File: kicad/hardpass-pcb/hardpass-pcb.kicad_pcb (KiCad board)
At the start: 2 copper layers, 80 x 65 mm, 61 parts, among them P1 Pi_Zero, P2 OLED_I2C, P3 Pi_Zero, SW1 1, SW10 C/UP, SW11 0/OK, SW12 OK/DN, SW2 2, SW3 3, SW4 4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

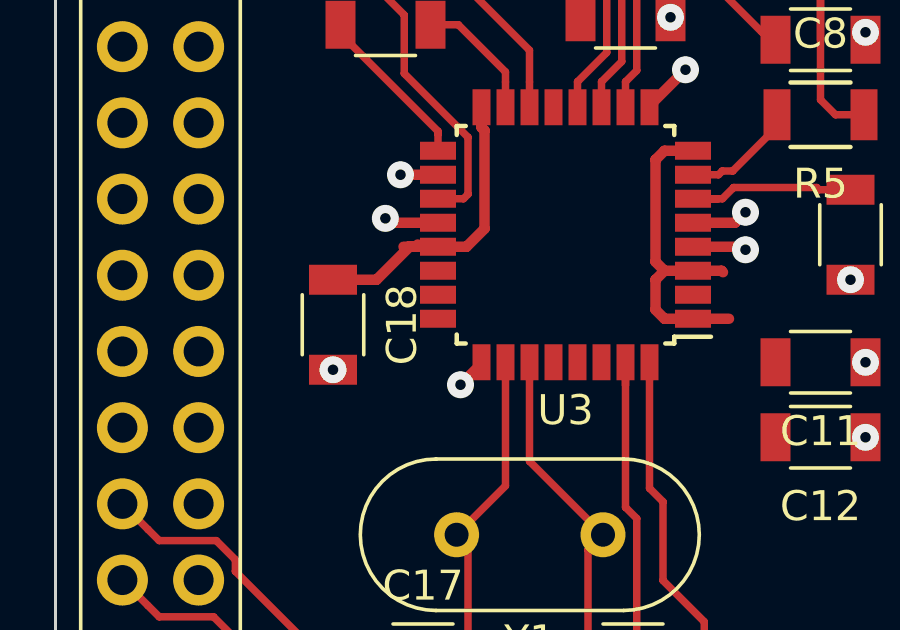
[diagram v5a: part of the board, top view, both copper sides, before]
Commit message: fixed bug (shdn_N), removed caps
according to data sheet, shdn_n needs to be high to activate card (page43)

2 bypass caps have been removed according to page 8 of AN00046
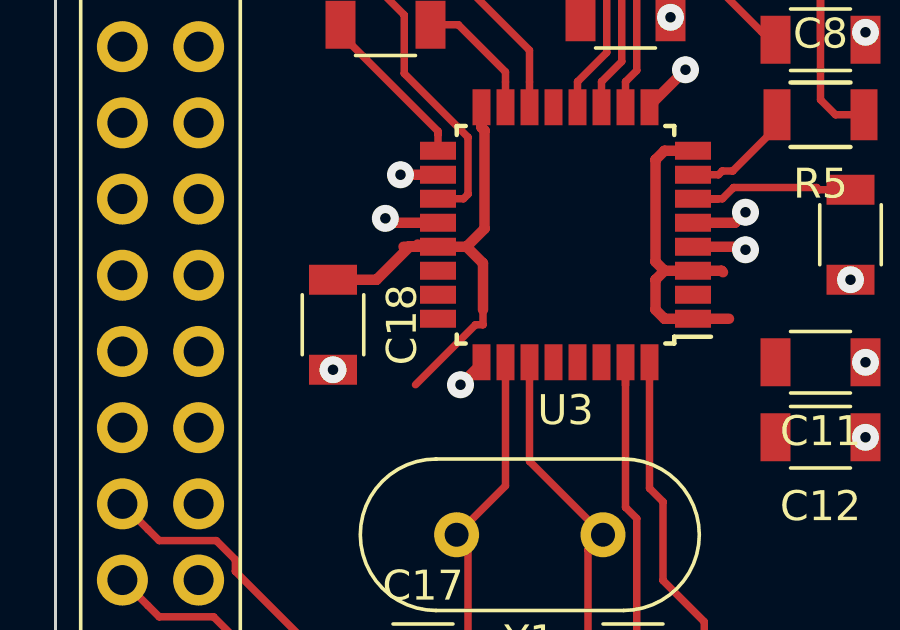
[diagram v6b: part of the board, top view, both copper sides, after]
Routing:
- net +5V: track 23.3 -> 29.2 mm
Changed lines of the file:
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@@
     (thickness 1.6)
     (drawings 26)
-    (tracks 712)
+    (tracks 717)
     (zones 0)
     (modules 61)
@@
   (segment (start 68.375001 25.680001) (end 68.375001 31.424999) (width 0.25) (layer F.Cu) (net 71))
   (segment (start 67.4 32.4) (end 67.4 33.25) (width 0.25) (layer F.Cu) (net 71))
+  (segment (start 64.25 40.5) (end 64 40.5) (width 0.25) (layer F.Cu) (net 72))
+  (segment (start 64 40.5) (end 62 42.5) (width 0.25) (layer F.Cu) (net 72))
+  (segment (start 64.25 40) (end 64.25 40.5) (width 0.25) (layer F.Cu) (net 72))
+  (segment (start 64.25 38.45) (end 64.25 40) (width 0.35) (layer F.Cu) (net 72))
+  (segment (start 63.7 37.9) (end 64.25 38.45) (width 0.35) (layer F.Cu) (net 72))
   (segment (start 70 35) (end 70 38.4) (width 0.35) (layer F.Cu) (net 72))
   (segment (start 70.3 38.7) (end 71.25 38.7) (width 0.35) (layer F.Cu) (net 72))

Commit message: board design work
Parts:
- removed C10: 100pF, Capacitors_SMD:C_1206
- removed C9: 33pF, Capacitors_SMD:C_1206
- moved C19 29.7 mm to (58.8, 34.8), turned to 270 degrees
- moved C14 2.50 mm to (75.5, 28.5)
- moved C8 2.50 mm to (75.5, 31.0)
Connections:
- U1 pad : (no net) -> GND
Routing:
- net +5V: track 29.2 -> 36.1 mm, vias 0 -> 2
- net Net-(C9-Pad1): track 13.3 -> 6.60 mm
- net Net-(C14-Pad2): track 34.9 -> 37.4 mm
- net GND: vias 17 -> 21
- net (no net): vias 4 -> 0

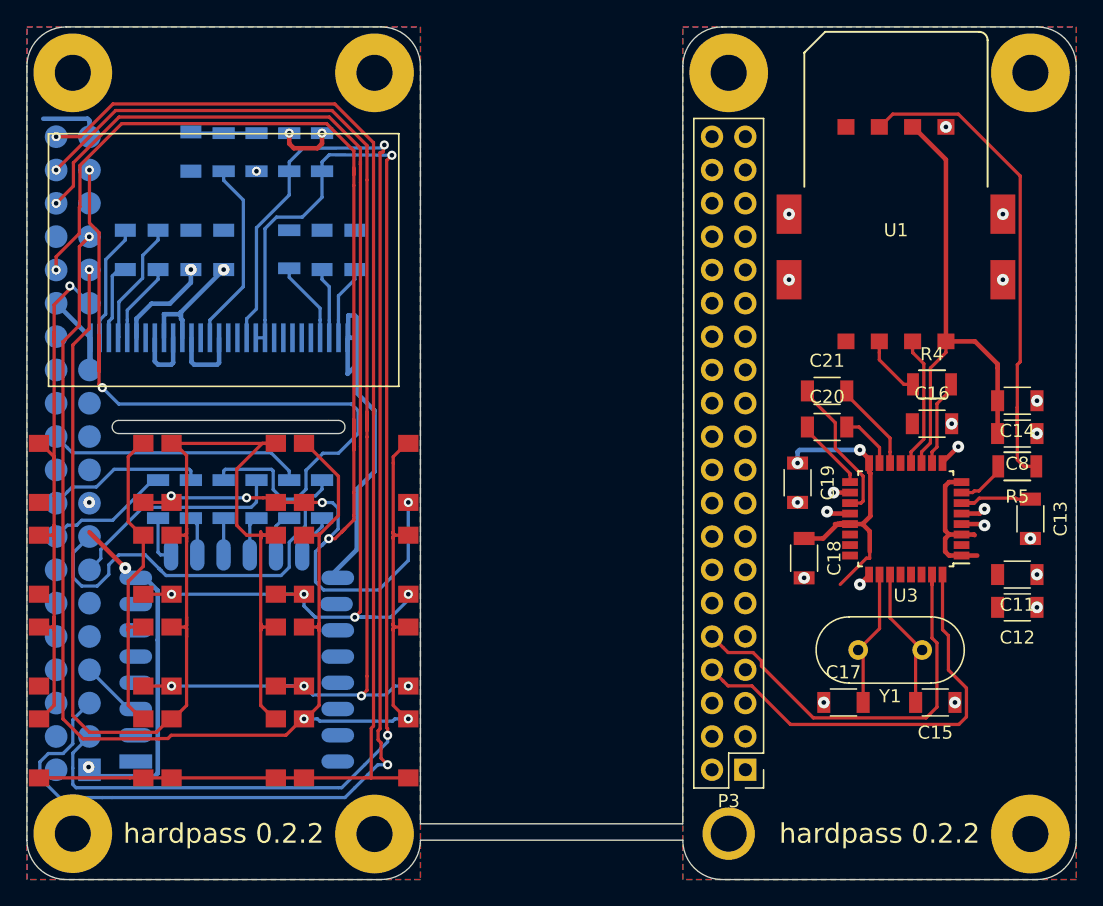
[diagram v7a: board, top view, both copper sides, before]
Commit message: cleanup, but accidentally deleted smartcard-pcb
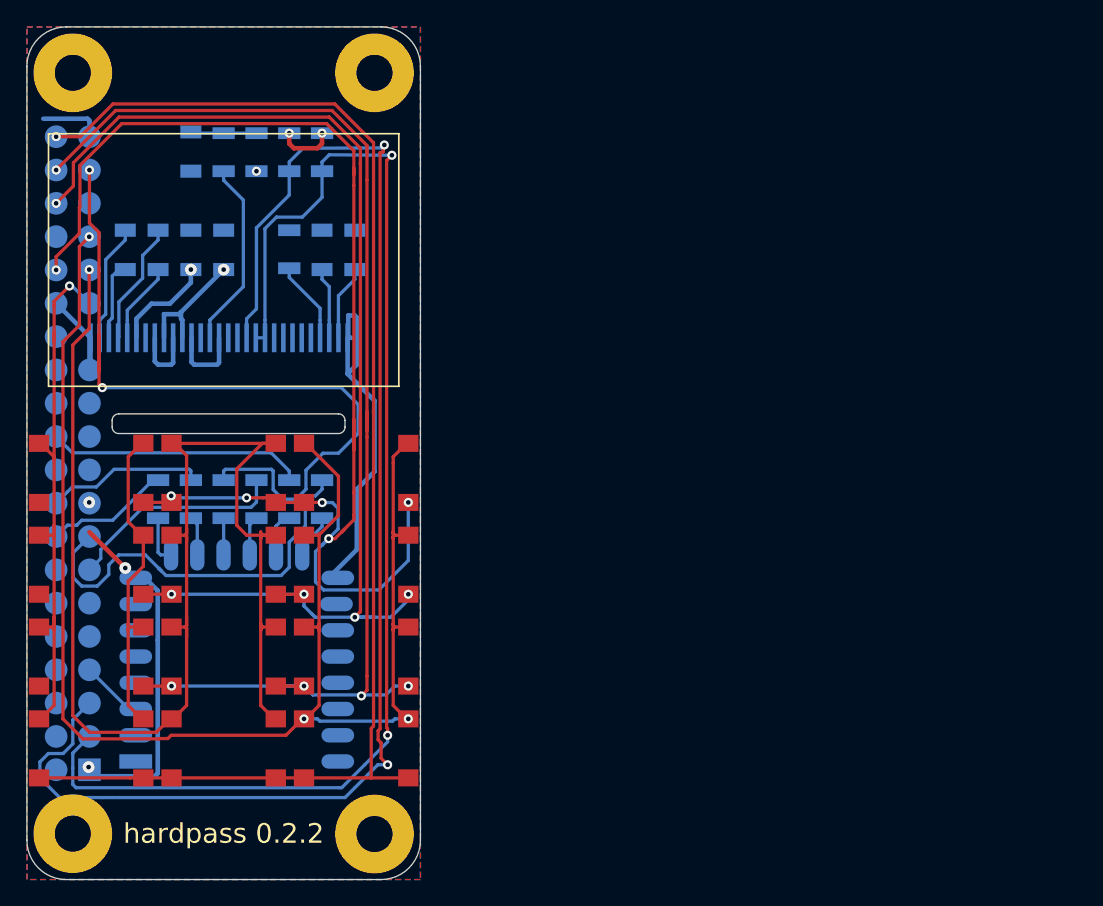
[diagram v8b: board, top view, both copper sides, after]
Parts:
- removed C11, C19: 10µF, Capacitors_SMD:C_1206
- removed C12, C18: 100nF, Capacitors_SMD:C_1206
- removed C13: 22nF, Capacitors_SMD:C_1206
- removed C14: 100pF, Capacitors_SMD:C_1206
- removed C15, C17: 22pF, Capacitors_SMD:C_1206
- removed C16, C20, C21, C8: 220nF, Capacitors_SMD:C_1206
- removed P3: Pi_Zero, hardpass:Pin_Header_Straight_2x20_Pitch2.54mm_centered
- removed R4: 100, Resistors_SMD:R_1206
- removed R5: 180, Resistors_SMD:R_1206
- removed the REF** at (76.5, 61.5)
- removed the REF** at (76.5, 3.50)
- removed the REF** at (53.5, 3.50)
- removed the REF** at (53.5, 61.5)
- removed U1: ISO7816, hardpass:CAF99-08153-S132
- removed U3: TDA8029, Housings_QFP:LQFP-32_7x7mm_Pitch0.8mm
- removed Y1: 14.745MHz, Crystals:Crystal_HC49-U_Vertical
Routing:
- net Net-(R5-Pad1): track 38.5 -> 0.00 mm
- net Net-(C14-Pad2): track 37.4 -> 0.00 mm
- net +5V: track 36.1 -> 0.00 mm, vias 2 -> 0
- net CARD_RX: track 33.0 -> 0.00 mm
- net CARD_TX: track 31.3 -> 0.00 mm
- net Net-(C21-Pad1): track 11.2 -> 0.00 mm
- net Net-(C15-Pad2): track 11.0 -> 0.00 mm
- net Net-(C17-Pad2): track 10.6 -> 0.00 mm
- net Net-(C10-Pad2): track 10.0 -> 0.00 mm
- net GND: track 62.5 -> 52.5 mm, vias 21 -> 0
- net Net-(C21-Pad2): track 6.87 -> 0.00 mm
- net Net-(C9-Pad1): track 6.60 -> 0.00 mm
- net Net-(C13-Pad1): track 6.29 -> 0.00 mm
- net Net-(C20-Pad1): track 5.55 -> 0.00 mm
- net Net-(R4-Pad1): track 4.75 -> 0.00 mm
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- removed copper zone on F.Cu, net +5V
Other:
- board size 80 x 65 mm -> 30 x 65 mm
